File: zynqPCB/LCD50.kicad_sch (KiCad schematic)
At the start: 16 parts, among them J4 HDMI_A, U19 PCA9306, U20B1 xc7z020clg484, U20D1 xc7z020clg484, U20E1 xc7z020clg484

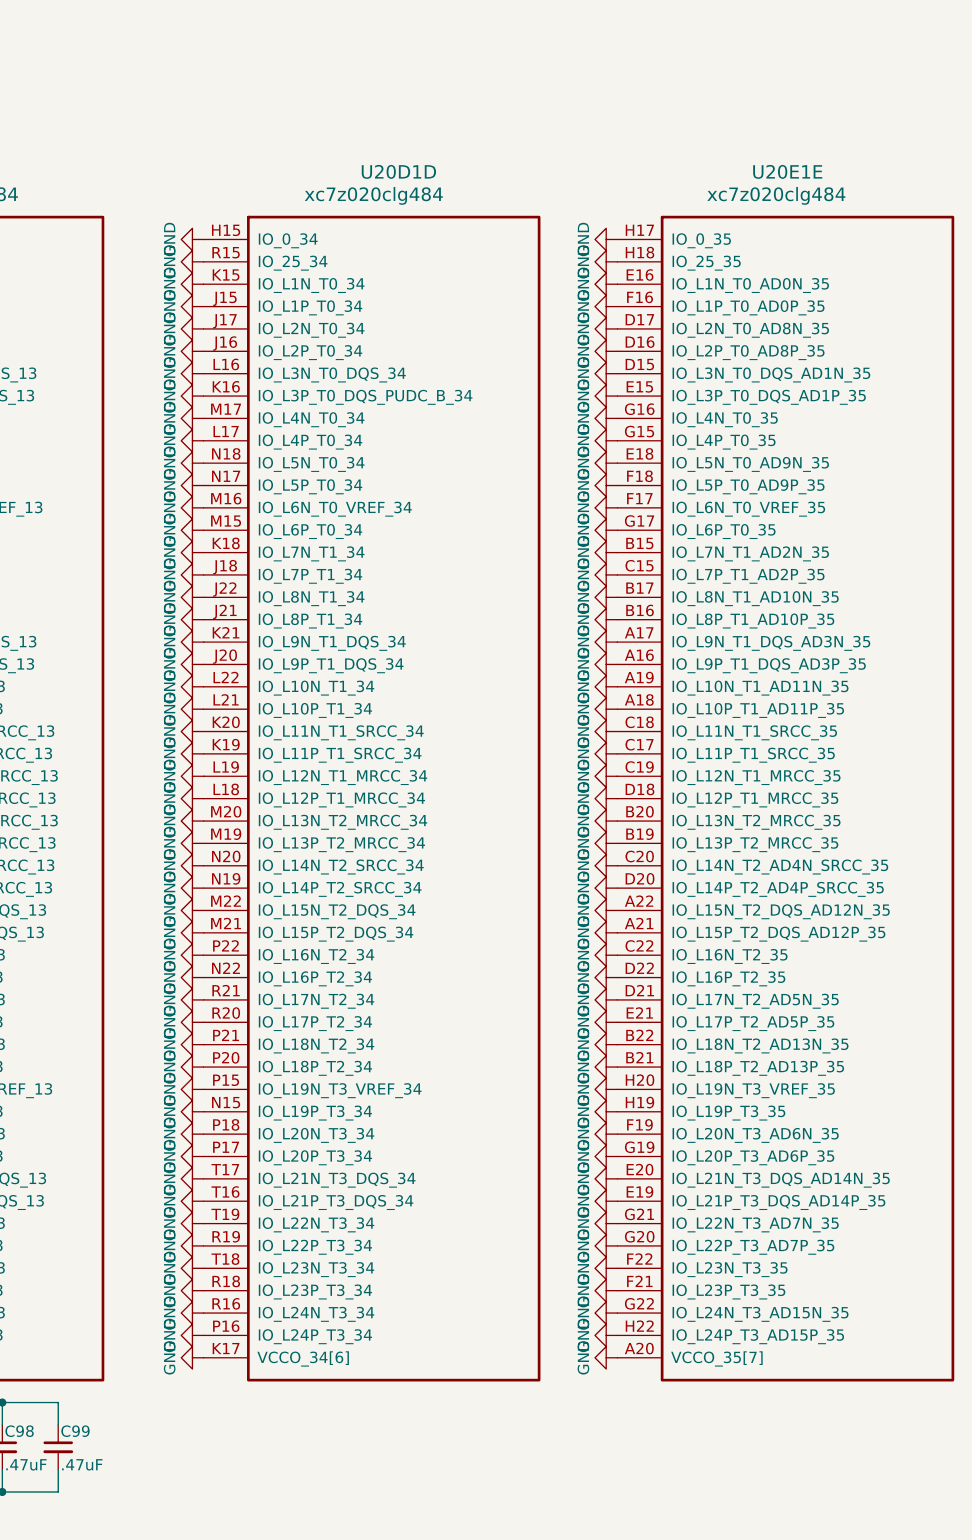
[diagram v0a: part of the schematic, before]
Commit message: Camera added
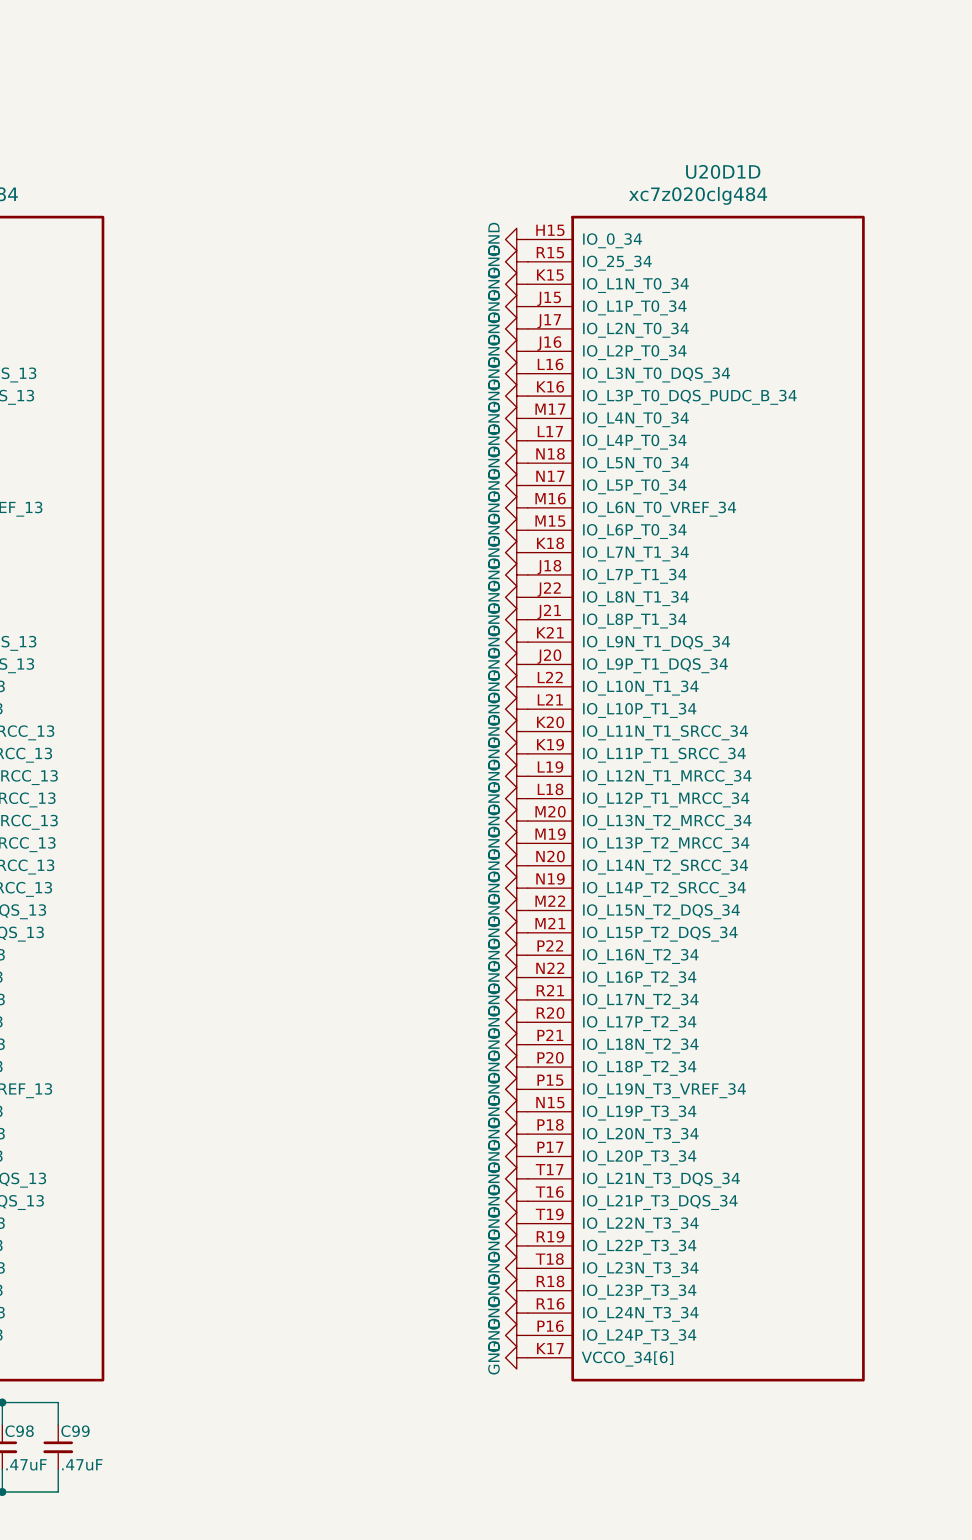
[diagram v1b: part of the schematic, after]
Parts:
- removed U20E1: xc7z020clg484, DFTcustom:BGA-484_19.0x19.0mm_Layout22x22_P0.80mm_dia0.40mm, symbol xilinx7:xc7z020clg484
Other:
- moved on the sheet: U20D1D
